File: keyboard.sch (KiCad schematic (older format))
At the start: 19 parts, among them CN2 KEYBOARD_HEADER, U13 MOS_6529

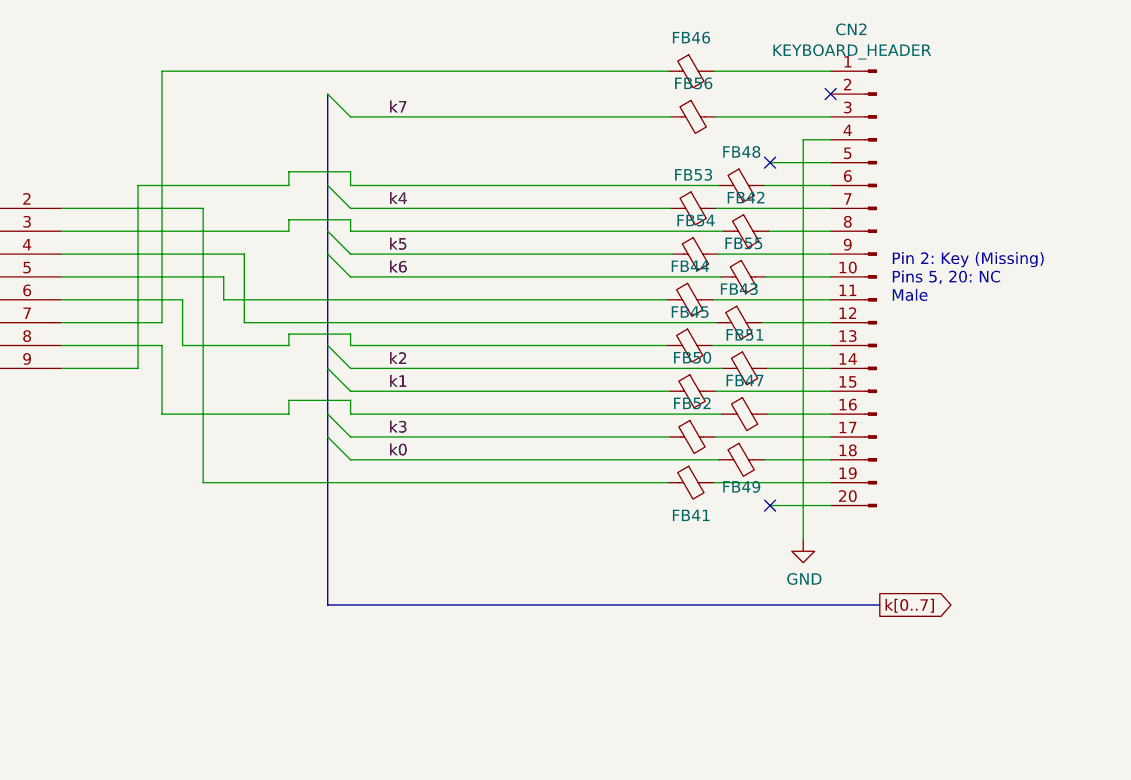
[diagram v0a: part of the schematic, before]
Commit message: Add buffers on joystick ports - WIP
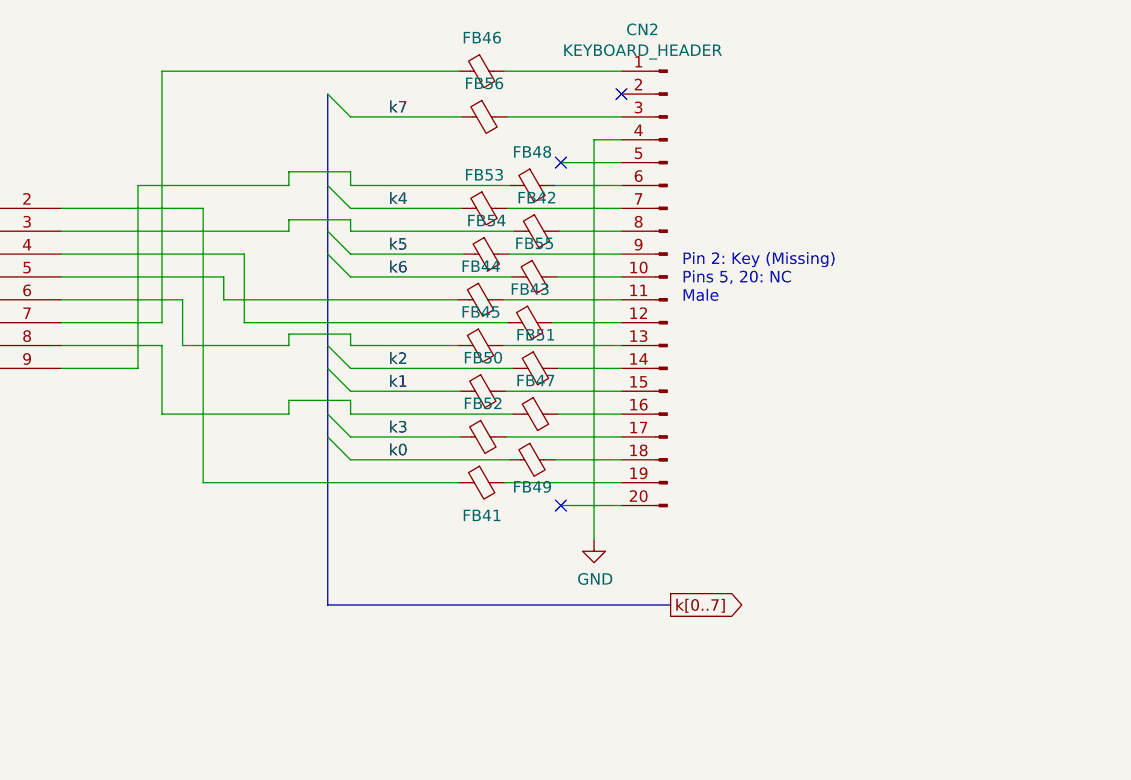
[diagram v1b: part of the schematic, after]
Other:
- moved on the sheet: CN2, FB41, FB42, FB43, FB44, FB45, FB46, FB47, FB48, FB49, FB50, FB51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

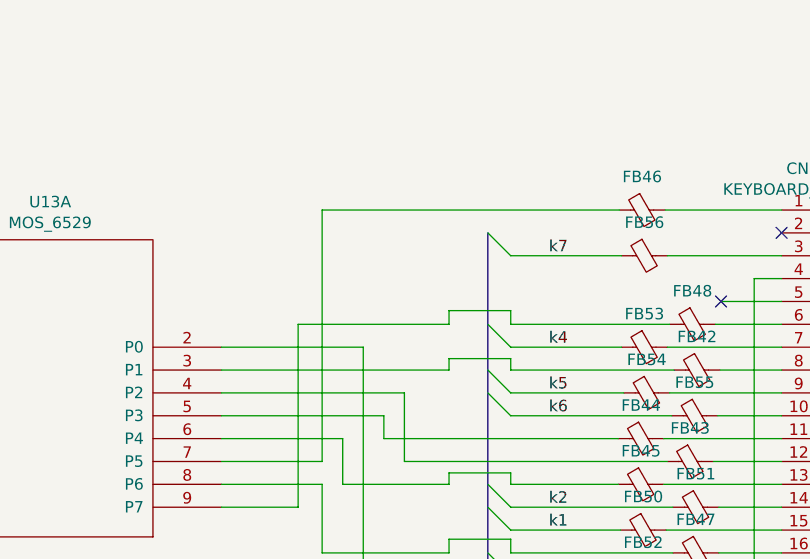
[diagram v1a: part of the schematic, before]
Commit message: Restore JD1/2
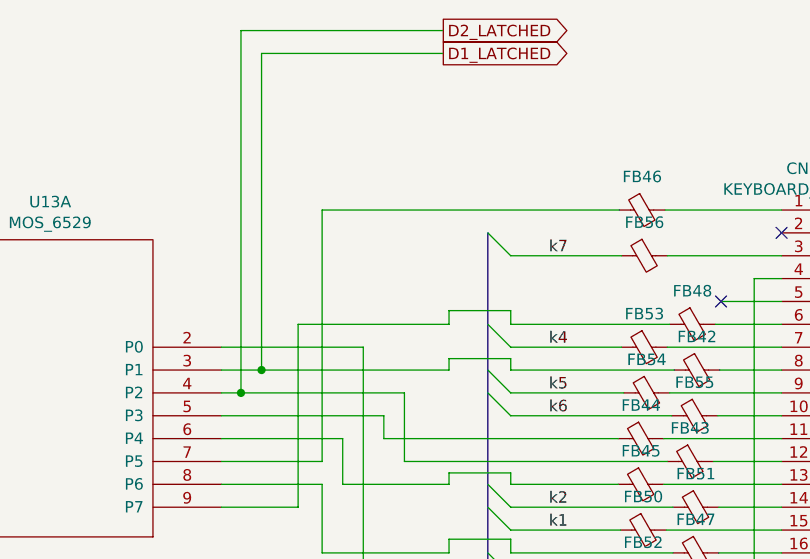
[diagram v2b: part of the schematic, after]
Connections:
- net D1_LATCHED: now reaches FB42.1, U13.3 (P1)
- net D2_LATCHED: now reaches FB43.1, U13.4 (P2)
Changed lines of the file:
@@
 	4005 3120 4760 3120
 Wire Wire Line
-	6260 3220 7060 3220
+	6260 3220 6345 3220
 Wire Wire Line
-	6260 3120 7255 3120
+	6260 3120 6435 3120
+Wire Wire Line
+	6435 3120 6435 1735
+Wire Wire Line
+	6435 1735 7230 1735
+Connection ~ 6435 3120
+Wire Wire Line
+	6435 3120 7255 3120
+Wire Wire Line
+	6345 3220 6345 1635
+Wire Wire Line
+	6345 1635 7230 1635
+Connection ~ 6345 3220
+Wire Wire Line
+	6345 3220 7060 3220
+Text GLabel 7230 1635 2    50   Output ~ 0
+D2_LATCHED
 Wire Bus Line
 	3905 2920 3905 3625
 Wire Bus Line
 	7425 2520 7425 4755
+Text GLabel 7230 1735 2    50   Output ~ 0
+D1_LATCHED
 $EndSCHEMATC

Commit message: Enlarge drill holes to 0.9mm in order to make it possible to use ZIF sockets
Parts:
- U13: footprint Package_DIP:DIP-20_W7.62mm_Socket_LongPads -> LittleSixteen:DIP-20_W7.62mm_Socket_LongPads
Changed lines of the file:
@@
 F 0 "U13" H 5510 4015 50  0000 C CNN
 F 1 "MOS_6529" H 5510 3924 50  0000 C CNN
-F 2 "Package_DIP:DIP-20_W7.62mm_Socket_LongPads" H 5510 3200 50  0001 C CNN
+F 2 "LittleSixteen:DIP-20_W7.62mm_Socket_LongPads" H 5510 3200 50  0001 C CNN
 F 3 "DOCUMENTATION" H 5510 3200 50  0001 C CNN
 	1    5510 3200
@@
 F 0 "U13" H 1077 6626 50  0000 R CNN
 F 1 "MOS_6529" H 1077 6535 50  0000 R CNN
-F 2 "Package_DIP:DIP-20_W7.62mm_Socket_LongPads" H 1345 6580 50  0001 C CNN
+F 2 "LittleSixteen:DIP-20_W7.62mm_Socket_LongPads" H 1345 6580 50  0001 C CNN
 F 3 "DOCUMENTATION" H 1345 6580 50  0001 C CNN
 	2    1345 6580

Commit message: Use local Ferrite_Bead_Small symbol
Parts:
- FB41, FB42, FB43, FB44, FB45, FB46, FB47, FB48, FB49, FB50, FB51, FB52, FB53, FB54, FB55, FB56: symbol Device:Ferrite_Bead_Small -> ferrite_bead_small:Ferrite_Bead_Small
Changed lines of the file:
@@
 	7525 3220 8020 3220
 $Comp
-L Device:Ferrite_Bead_Small FB46
+L ferrite_bead_small:Ferrite_Bead_Small FB46
 U 1 1 5E275829
 P 8100 2420
@@
 	8200 2420 8710 2420
 $Comp
-L Device:Ferrite_Bead_Small FB56
+L ferrite_bead_small:Ferrite_Bead_Small FB56
 U 1 1 5E277735
 P 8110 2620
@@
 	8710 2820 8445 2820
 $Comp
-L Device:Ferrite_Bead_Small FB53
+L ferrite_bead_small:Ferrite_Bead_Small FB53
 U 1 1 5E279505
 P 8110 3020
@@
 	8210 3020 8710 3020
 $Comp
-L Device:Ferrite_Bead_Small FB54
+L ferrite_bead_small:Ferrite_Bead_Small FB54
 U 1 1 5E27AC84
 P 8120 3220
@@
 	8220 3220 8710 3220
 $Comp
-L Device:Ferrite_Bead_Small FB44
+L ferrite_bead_small:Ferrite_Bead_Small FB44
 U 1 1 5E27B4EF
 P 8095 3420
@@
 	8195 3420 8710 3420
 $Comp
-L Device:Ferrite_Bead_Small FB45
+L ferrite_bead_small:Ferrite_Bead_Small FB45
 U 1 1 5E27BE11
 P 8095 3620
@@
 	8195 3620 8710 3620
 $Comp
-L Device:Ferrite_Bead_Small FB50
+L ferrite_bead_small:Ferrite_Bead_Small FB50
 U 1 1 5E27C5F0
 P 8105 3820
@@
 	8205 3820 8710 3820
 $Comp
-L Device:Ferrite_Bead_Small FB52
+L ferrite_bead_small:Ferrite_Bead_Small FB52
 U 1 1 5E27CC99
 P 8105 4020
@@
 	8205 4020 8710 4020
 $Comp
-L Device:Ferrite_Bead_Small FB41
+L ferrite_bead_small:Ferrite_Bead_Small FB41
 U 1 1 5E27D4CD
 P 8100 4220
@@
 	8200 4220 8710 4220
 $Comp
-L Device:Ferrite_Bead_Small FB48
+L ferrite_bead_small:Ferrite_Bead_Small FB48
 U 1 1 5E27E7DF
 P 8320 2920
@@
 	8420 2920 8710 2920
 $Comp
-L Device:Ferrite_Bead_Small FB42
+L ferrite_bead_small:Ferrite_Bead_Small FB42
 U 1 1 5E27ED7A
 P 8340 3120
@@
 	8440 3120 8710 3120
 $Comp
-L Device:Ferrite_Bead_Small FB55
+L ferrite_bead_small:Ferrite_Bead_Small FB55
 U 1 1 5E27F5BE
 P 8330 3320
@@
 	8430 3320 8710 3320
 $Comp
-L Device:Ferrite_Bead_Small FB43
+L ferrite_bead_small:Ferrite_Bead_Small FB43
 U 1 1 5E27FD6B
 P 8310 3520
@@
 	8410 3520 8710 3520
 $Comp
-L Device:Ferrite_Bead_Small FB51
+L ferrite_bead_small:Ferrite_Bead_Small FB51
 U 1 1 5E280D1A
 P 8335 3720
@@
 	8435 3720 8710 3720
 $Comp
-L Device:Ferrite_Bead_Small FB47
+L ferrite_bead_small:Ferrite_Bead_Small FB47
 U 1 1 5E281382
 P 8335 3920
@@
 	8435 3920 8710 3920
 $Comp
-L Device:Ferrite_Bead_Small FB49
+L ferrite_bead_small:Ferrite_Bead_Small FB49
 U 1 1 5E2818F5
 P 8320 4120

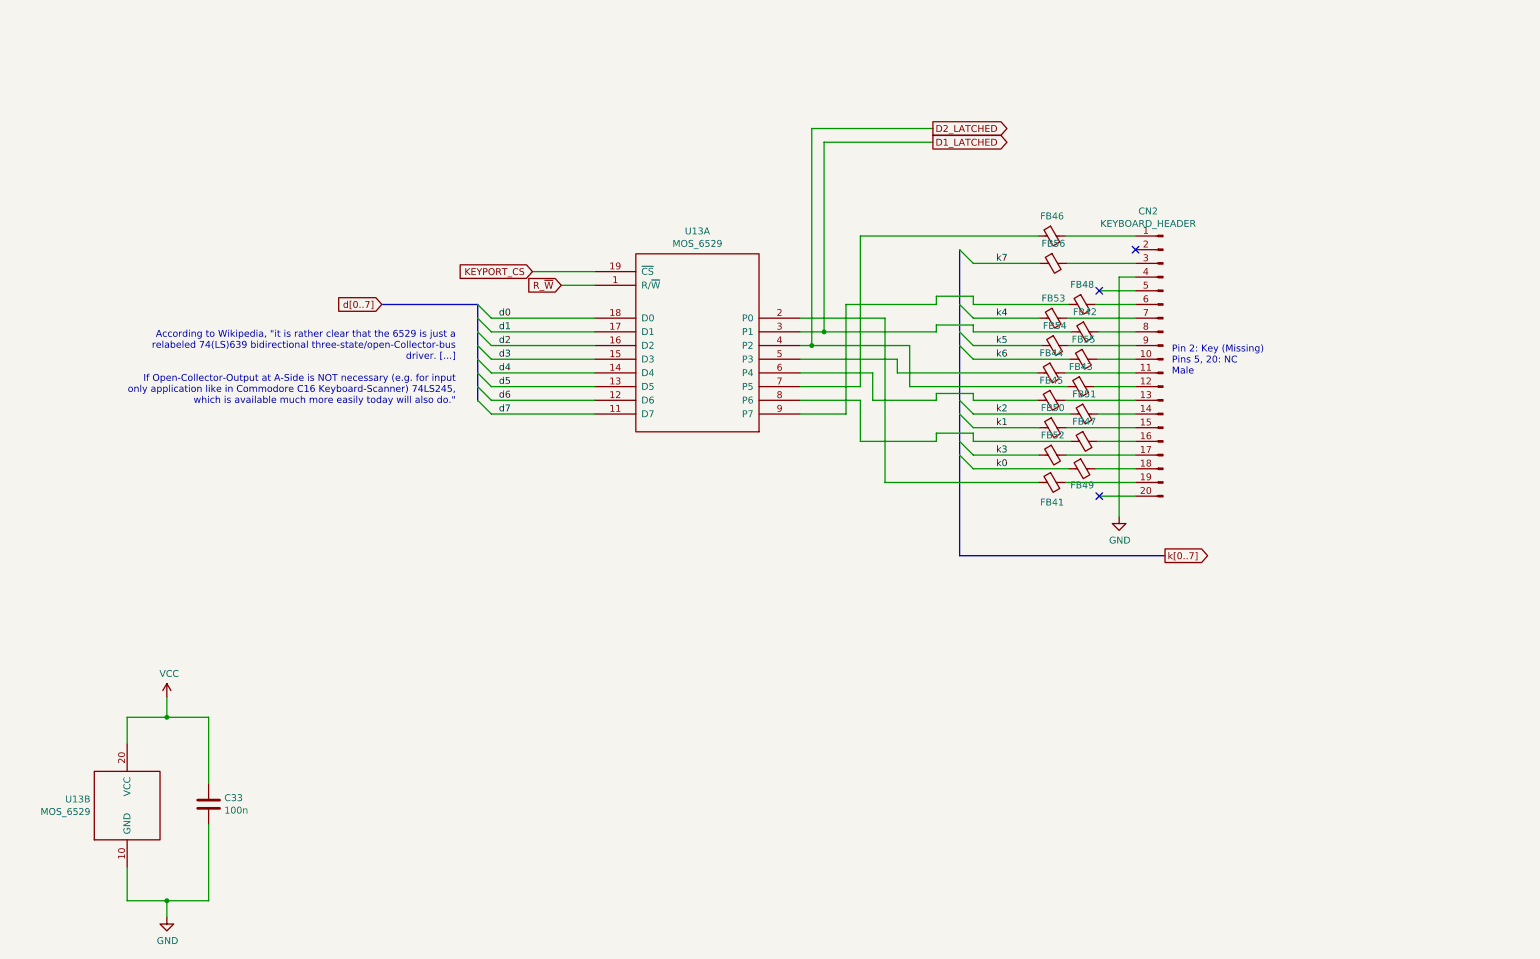
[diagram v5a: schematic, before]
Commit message: Design a working alternative for MOS6529
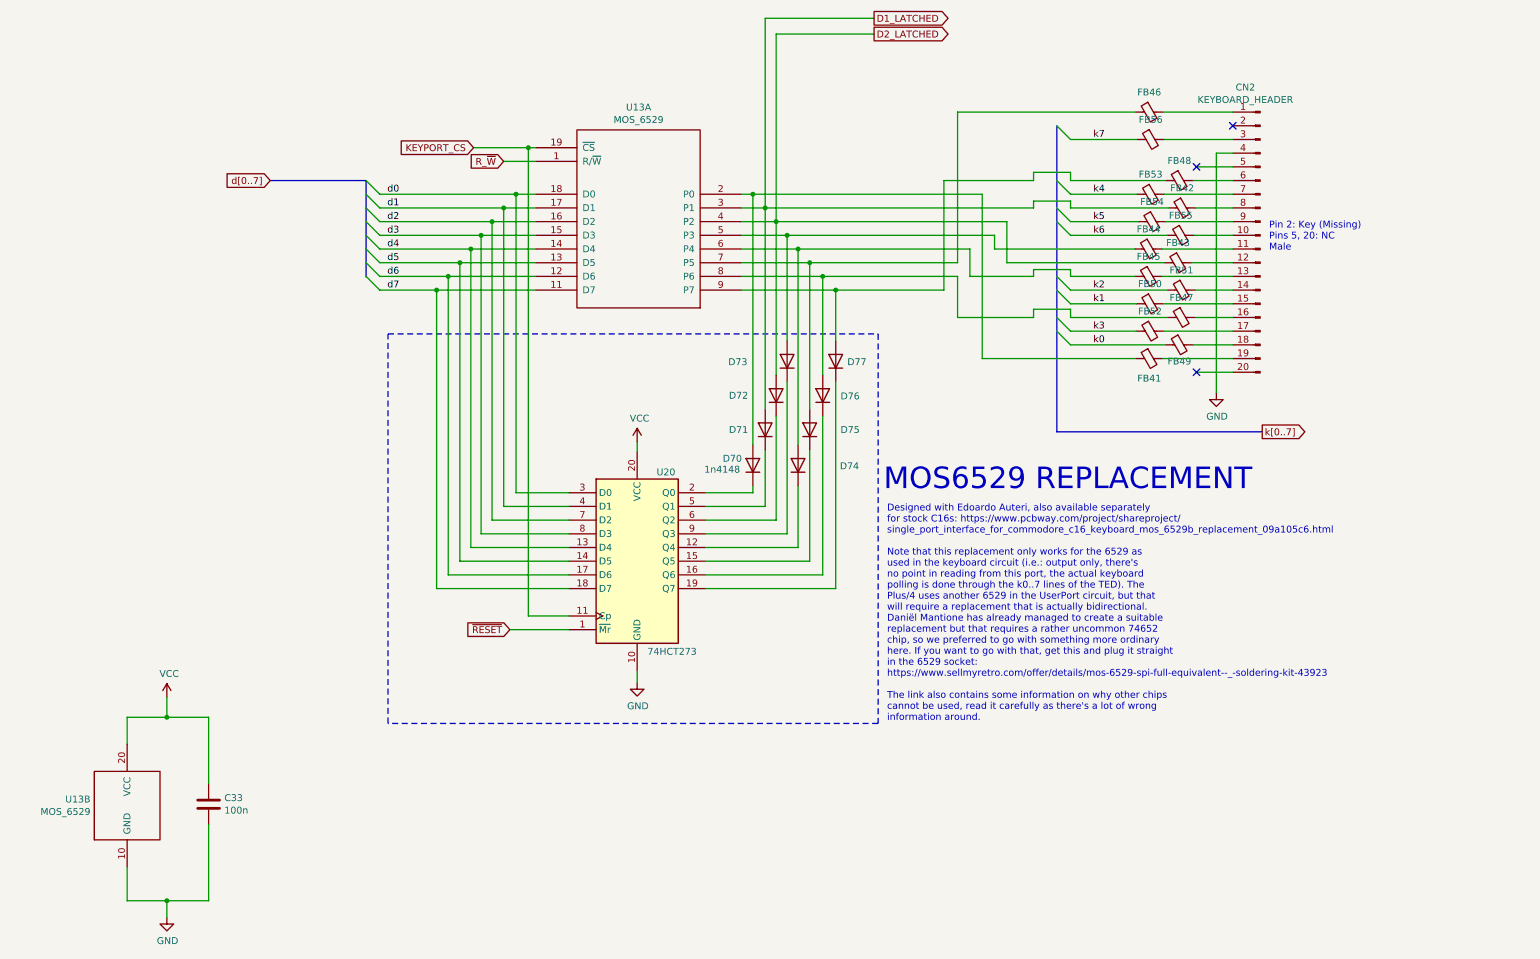
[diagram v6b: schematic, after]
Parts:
- added D70, D71, D72, D73, D74, D75, D76, D77: 1n4148, LittleSixteen:D_DO-35_SOD27_P5.08mm_Vertical_KathodeUp, symbol Device:D
- added U20: 74HCT273, symbol 74xx:74HCT273
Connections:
- net D1_LATCHED: now also D71.2 (A)
- net D2_LATCHED: now also D72.2 (A)
- net GND: now also U20.10 (GND)
- net KEYPORT_CS: now also U20.11 (Cp)
- net VCC: now also U20.20 (VCC)
- net d0: now also U20.3 (D0)
- net d1: now also U20.4 (D1)
- net d2: now also U20.7 (D2)
- net d3: now also U20.8 (D3)
- net d4: now also U20.13 (D4)
- net d5: now also U20.14 (D5)
- net d6: now also U20.17 (D6)
- net d7: now also U20.18 (D7)
- net at FB41.1, U13.2 (P0): now also D70.2 (A)
- net at FB44.1, U13.5 (P3): now also D73.2 (A)
- net at FB45.1, U13.6 (P4): now also D74.2 (A)
- net at FB46.1, U13.7 (P5): now also D75.2 (A)
- net at FB47.1, U13.8 (P6): now also D76.2 (A)
- net at FB48.1, U13.9 (P7): now also D77.2 (A)
- new net: D74.1 (K), U20.12 (Q4)
- new net: D75.1 (K), U20.15 (Q5)
- new net: D76.1 (K), U20.16 (Q6)
- new net: D77.1 (K), U20.19 (Q7)
- new net: D70.1 (K), U20.2 (Q0)
- new net: D71.1 (K), U20.5 (Q1)
- new net: D72.1 (K), U20.6 (Q2)
- new net: D73.1 (K), U20.9 (Q3)
- new net ~RESET: U20.1 (~Mr)
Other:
- note added: "Designed with Edoardo Auteri, also available separately\nfor stock C16s: https://www.pcbway.com/project/shareproject/\nsingle_port_interface_for_commodore_c16_keyboard_mos_6529b_replacement_09a105c6.html\n\nNote that this replacement only works for the 6529 as\nused in the keyboard circuit (i.e.: output only, there's\nno point in reading from this port, the actual keyboard\npolling is done throug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"
- note added: "MOS6529 REPLACEMENT"
- note removed: "According to Wikipedia, "it is rather clear that the 6529 is just a\nrelabeled 74(LS)639 bidirectional three-state/open-Collector-bus\ndriver. [...]\n\nIf Open-Collector-Output at A-Side is NOT necessary (e.g. for input\nonly application like in Commodore C16 Keyboard-Scanner) 74LS245,\nwhich is available much more easily today will also do.""
- moved on the sheet: CN2, FB41, FB42, FB43, FB44, FB45, FB46, FB47, FB48, FB49, FB50, FB51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
